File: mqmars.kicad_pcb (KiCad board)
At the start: 2 copper layers, 275 parts, among them Q1 GSFP6016, Q10 GSFP6016, Q11 GSFP6016, Q12 GSFP6016, Q13 GSFP6016, Q14 GSFP6016, Q15 GSFP6016, Q16 GSFP6016, Q17 GSFP6016, Q18 GSFP6016, Q19 GSFP6016, Q2 GSFP6016, Q20 GSFP6016, Q21 GSFP6016, Q22 GSFP6016, Q23 GSFP6016, Q24 GSFP6016, Q25 GSFP6016, Q26 GSFP6016, Q27 GSFP6016, Q28 GSFP6016, Q29 GSFP6016, Q3 GSFP6016, Q30 GSFP6016, Q31 GSFP6016, Q32 GSFP6016, Q33 GSFP6016, Q34 GSFP6016, Q35 GSFP6016, Q36 GSFP6016, Q37 BC846, Q38 BC846, Q39 G700P06D5, Q4 GSFP6016, Q40 G700P06D5, Q41 BC846, Q42 BC846, Q43 G700P06D5, Q44 G700P06D5, Q45 BC846, Q46 BC846, Q47 G700P06D5, Q48 G700P06D5, Q5 GSFP6016, Q6 GSFP6016, Q7 GSFP6016, Q8 GSFP6016, Q9 GSFP6016, U1 MCT8329A1IREER, U10 TCA9548APWR, U12 TPS56224, U13 LMV358, U2 MCT8329A1IREER, U3 MCT8329A1IREER, U4 MCT8329A1IREER, U5 MCT8329A1IREER, U6 MCT8329A1IREER, U8 MCP23017_SO, U9 TLA2528IRTER

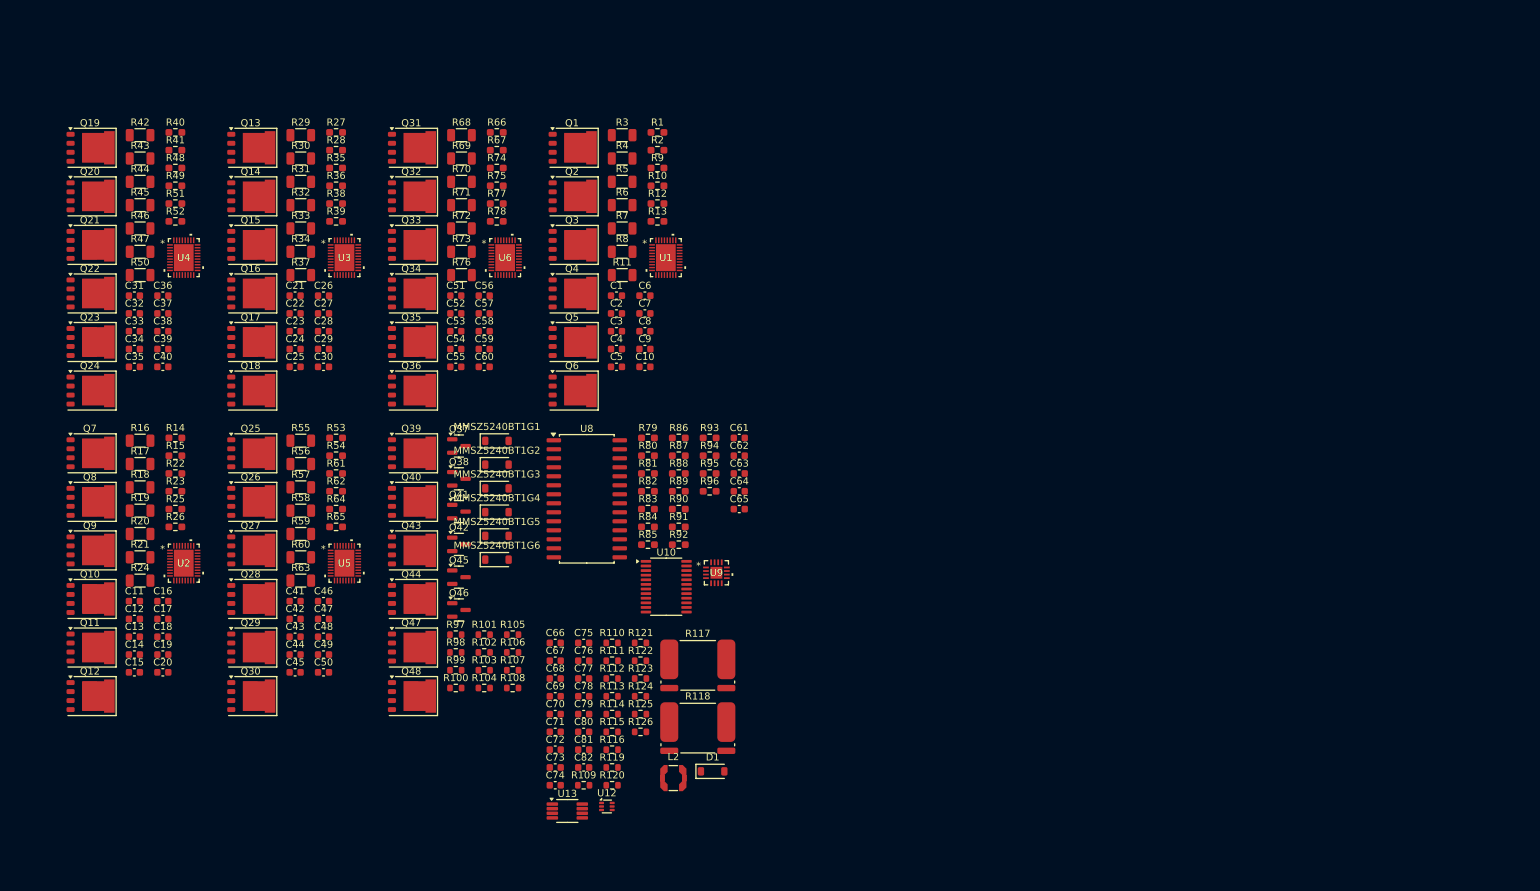
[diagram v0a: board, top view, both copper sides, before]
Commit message: Powerstage
Powerstage layout, non critical changes to schematic
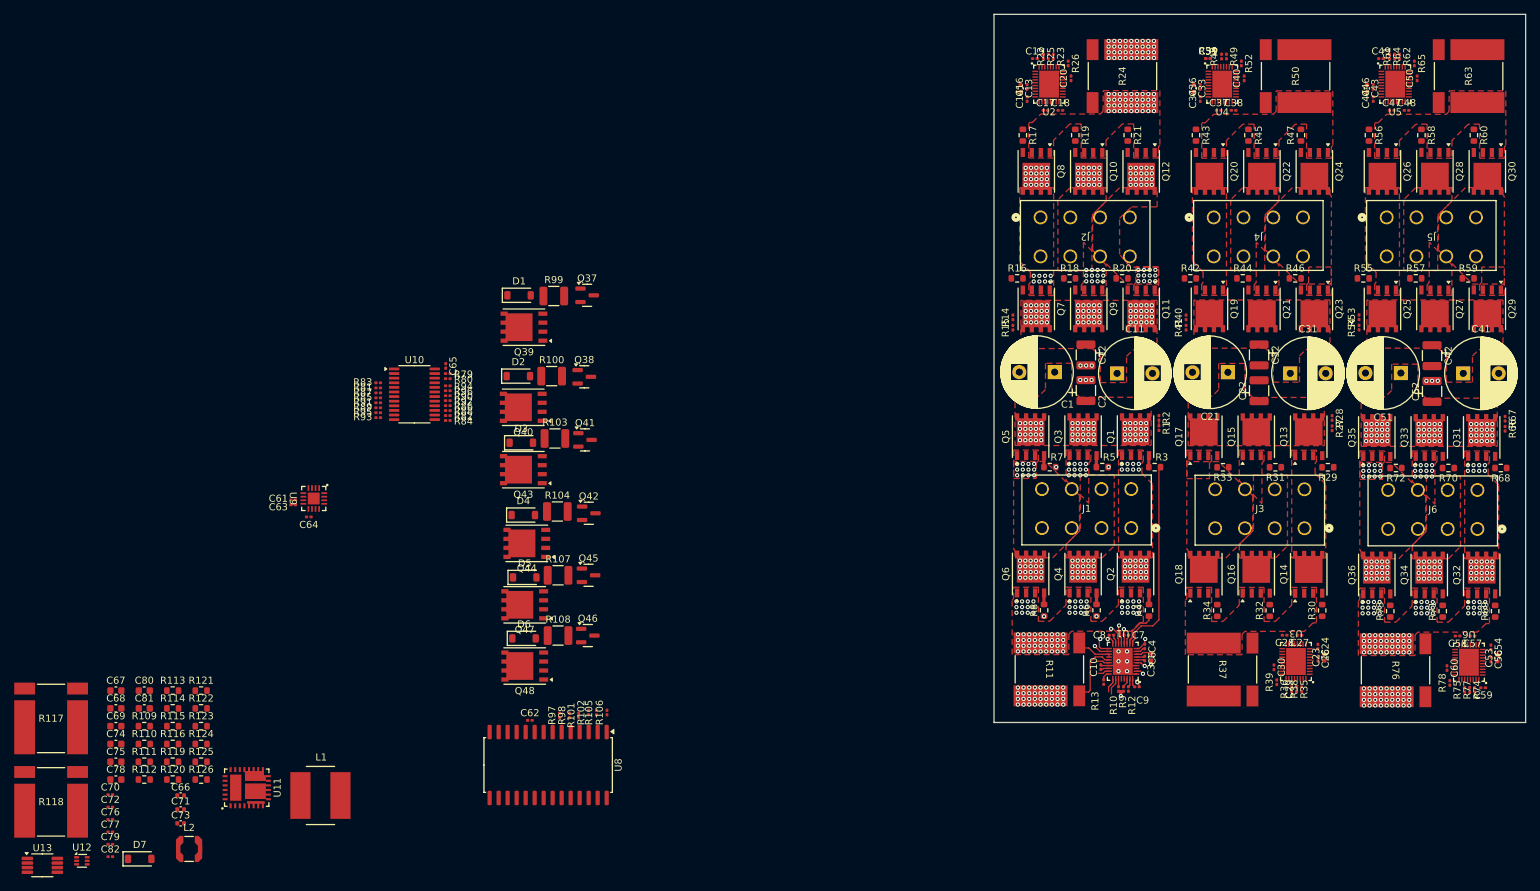
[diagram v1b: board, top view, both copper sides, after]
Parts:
- removed C15, C25, C35, C45, C5, C55: 100n, Capacitor_SMD:C_0603_1608Metric
- removed MMSZ5240BT1G1, MMSZ5240BT1G2, MMSZ5240BT1G3, MMSZ5240BT1G4, MMSZ5240BT1G5, MMSZ5240BT1G6: 10V1, Diode_SMD:D_SOD-123
- added D2: 10V1, Diode_SMD:D_SOD-123, F.Cu at (124.4, 76.5)
- added D3: 10V1, Diode_SMD:D_SOD-123, F.Cu at (124.8, 85.9)
- added D4: 10V1, Diode_SMD:D_SOD-123, F.Cu at (125.1, 96.1)
- added D5: 10V1, Diode_SMD:D_SOD-123, F.Cu at (125.3, 104.9)
- added D6: 10V1, Diode_SMD:D_SOD-123, F.Cu at (125.2, 113.5)
- added D7: SD103AW, Diode_SMD:D_SOD-123, F.Cu at (71.0, 144.6)
- added J1: 1724470408, footprints:CONN08_1724470408_MOL, F.Cu at (210.9, 98.0)
- added J2: 1724470408, footprints:CONN08_1724470408_MOL, F.Cu at (198.1, 54.1)
- added J3: 1724470408, footprints:CONN08_1724470408_MOL, F.Cu at (235.3, 98.0)
- added J4: 1724470408, footprints:CONN08_1724470408_MOL, F.Cu at (222.5, 54.1)
- added J5: 1724470408, footprints:CONN08_1724470408_MOL, F.Cu at (246.9, 54.1)
- added J6: 1724470408, footprints:CONN08_1724470408_MOL, F.Cu at (259.7, 98.1)
- added L1: 2.2u, Inductor_SMD:L_Bourns_SRN8040TA, F.Cu at (96.5, 135.7)
- added U11: MIC26903YJL-TR, footprints:MLF28_5X6_MCH, F.Cu at (86.1, 134.6)
- C1, C11, C21, C31, C41, C51: footprint Capacitor_SMD:C_0603_1608Metric -> Capacitor_THT:CP_Radial_D10.0mm_P5.00mm
- C10, C14, C16, C17, C18, C19, C20, C24, C26, C27, C28, C29, C30, C34, C36, C37, C38, C39, C4, C40, C44, C46, C47, C48, C49, C50, C54, C56, C57, C58, C59, C6, C60, C61, C62, C63, C64, C7, C70, C72, C76, C79, C8, C82, C9: footprint Capacitor_SMD:C_0603_1608Metric -> Capacitor_SMD:C_0201_0603Metric
- C12, C2, C22, C32, C42, C52: footprint Capacitor_SMD:C_0603_1608Metric -> Capacitor_SMD:C_1210_3225Metric
- C13, C23, C3, C33, C43, C53, C66, C71, C73: footprint Capacitor_SMD:C_0603_1608Metric -> Capacitor_SMD:C_0402_1005Metric
- C65: value 100n -> ~; footprint Capacitor_SMD:C_0603_1608Metric -> Capacitor_SMD:C_0201_0603Metric
- C77: value 4.7n -> ~; footprint Capacitor_SMD:C_0603_1608Metric -> Capacitor_SMD:C_0201_0603Metric
- D1: value SD103AW -> MMSZ5240BT1G5
- Q1, Q10, Q11, Q12, Q13, Q14, Q15, Q16, Q17, Q18, Q19, Q2, Q20, Q21, Q22, Q23, Q24, Q25, Q26, Q27, Q28, Q29, Q3, Q30, Q31, Q32, Q33, Q34, Q35, Q36, Q39, Q4, Q40, Q43, Q44, Q47, Q48, Q5, Q6, Q7, Q8, Q9: footprint Package_DFN_QFN:PQFN-8-EP_6x5mm_P1.27mm_Generic -> Package_SO:PowerPAK_SO-8_Single
- R1, R10, R12, R13, R14, R15, R2, R22, R23, R25, R26, R27, R28, R35, R36, R38, R39, R40, R41, R48, R49, R51, R52, R53, R54, R61, R62, R64, R65, R66, R67, R74, R75, R77, R78, R79, R80, R81, R82, R83, R84, R85, R86, R87, R88, R89, R9, R90, R91, R92, R93, R94, R95, R96: footprint Resistor_SMD:R_0603_1608Metric_Pad0.98x0.95mm_HandSolder -> Resistor_SMD:R_0201_0603Metric
- R100, R103, R104, R107, R108, R99: footprint Resistor_SMD:R_0603_1608Metric -> Resistor_SMD:R_1210_3225Metric
- R101, R102, R105, R106, R97, R98: footprint Resistor_SMD:R_0603_1608Metric -> Resistor_SMD:R_0201_0603Metric
- R11, R24, R37, R50, R63, R76: value 10m0R -> WSL3637R0100FEA; footprint Resistor_SMD:R_1206_3216Metric -> footprints:WSL3637_VIS
- R117, R118: value 10m0R -> WSL3637R0100FEA; footprint Resistor_SMD:R_Shunt_Isabellenhuette_BVR4026 -> footprints:WSL3637_VIS
- R16, R17, R18, R19, R20, R21, R29, R3, R30, R31, R32, R33, R34, R4, R42, R43, R44, R45, R46, R47, R5, R55, R56, R57, R58, R59, R6, R60, R68, R69, R7, R70, R71, R72, R73, R8: value 4.7R -> 4R7; footprint Resistor_SMD:R_1206_3216Metric -> Resistor_SMD:R_0603_1608Metric
- moved Q30 189.5 mm to (261.1, 47.7), turned to -90 degrees
- moved Q29 180.9 mm to (261.1, 67.0), turned to -90 degrees
- moved R63 179.5 mm to (258.5, 34.2), turned to 90 degrees
- moved Q28 177.6 mm to (253.7, 47.6), turned to -90 degrees
- moved R60 175.9 mm to (259.2, 42.5), turned to -90 degrees
- moved C50 175.6 mm to (251.2, 34.5), turned to 90 degrees
- moved Q24 175.5 mm to (236.7, 47.7), turned to -90 degrees
- moved Q23 172.8 mm to (236.7, 67.1), turned to -90 degrees
- moved C49 171.2 mm to (246.1, 31.7)
- moved C44 171.1 mm to (245.0, 37.4), turned to 90 degrees
- moved Q27 170.5 mm to (253.7, 67.1), turned to -90 degrees
- moved C48 169.9 mm to (249.7, 39.0)
- moved C43 169.8 mm to (244.1, 35.9), turned to -90 degrees
- moved R59 168.6 mm to (258.4, 62.7)
- moved C41 167.9 mm to (257.7, 76.1)
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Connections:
- C14 pad 1: Net-(J4-Pin_1) -> Net-(Q8-D)
- C16 pad 1: Net-(U2-CPL) -> Net-(U2-CPH)
- C16 pad 2: Net-(U2-CPH) -> Net-(U2-CPL)
- C17 pad 2: Net-(J5-Pin_1) -> Net-(Q10-D)
- C18 pad 2: Net-(J6-Pin_1) -> Net-(Q12-D)
- C24 pad 1: Net-(J7-Pin_1) -> Net-(Q14-D)
- C26 pad 1: Net-(U3-CPL) -> Net-(U3-CPH)
- C26 pad 2: Net-(U3-CPH) -> Net-(U3-CPL)
- C27 pad 2: Net-(J8-Pin_1) -> Net-(Q16-D)
- C28 pad 2: Net-(J9-Pin_1) -> Net-(Q18-D)
- C34 pad 1: Net-(J10-Pin_1) -> Net-(Q20-D)
- C36 pad 1: Net-(U4-CPL) -> Net-(U4-CPH)
- C36 pad 2: Net-(U4-CPH) -> Net-(U4-CPL)
- C37 pad 2: Net-(J11-Pin_1) -> Net-(Q22-D)
- C38 pad 2: Net-(J12-Pin_1) -> Net-(Q24-D)
- C4 pad 1: Net-(J1-Pin_1) -> Net-(Q2-D)
- C41 pad 1: Net-(U5-PVDD) -> RC_{VDD}
- C42 pad 1: Net-(U5-PVDD) -> RC_{VDD}
- C44 pad 1: Net-(J13-Pin_1) -> Net-(Q26-D)
- C46 pad 1: Net-(U5-CPL) -> Net-(U5-CPH)
- C46 pad 2: Net-(U5-CPH) -> Net-(U5-CPL)
- C47 pad 2: Net-(J14-Pin_1) -> Net-(Q28-D)
- C48 pad 2: Net-(J15-Pin_1) -> Net-(Q30-D)
- C54 pad 1: Net-(J16-Pin_1) -> Net-(Q32-D)
- C56 pad 1: Net-(U6-CPL) -> Net-(U6-CPH)
- C56 pad 2: Net-(U6-CPH) -> Net-(U6-CPL)
- C57 pad 2: Net-(J17-Pin_1) -> Net-(Q34-D)
- C58 pad 2: Net-(J18-Pin_1) -> Net-(Q36-D)
- C6 pad 1: Net-(U1-CPL) -> Net-(U1-CPH)
- C6 pad 2: Net-(U1-CPH) -> Net-(U1-CPL)
- C7 pad 2: Net-(J2-Pin_1) -> Net-(Q4-D)
- C70 pad 1: Net-(D1-K) -> Net-(D7-K)
- C73 pad 2: Net-(D1-A) -> Net-(D7-A)
- C8 pad 2: Net-(J3-Pin_1) -> Net-(Q6-D)
- D1 pad 1: Net-(D1-K) -> +BATT
- Q1 pad 1: +BATT -> Net-(Q2-D)
- Q1 pad 2: Net-(Q1-G) -> Net-(Q2-D)
- Q1 pad 3: Net-(J1-Pin_1) -> Net-(Q2-D)
- Q1 pad 4: (no net) -> Net-(Q1-G)
- Q1 pad 5: (no net) -> LF_{VDD}
- Q10 pad 1: Net-(J5-Pin_1) -> Net-(Q10-S-Pad1)
- Q10 pad 2: Net-(Q10-G) -> Net-(Q10-S-Pad1)
- Q10 pad 3: Net-(Q10-S) -> Net-(Q10-S-Pad1)
- Q10 pad 4: (no net) -> Net-(Q10-G)
- Q10 pad 5: (no net) -> Net-(Q10-D)
- Q11 pad 1: +BATT -> Net-(Q12-D)
- Q11 pad 2: Net-(Q11-G) -> Net-(Q12-D)
- Q11 pad 3: Net-(J6-Pin_1) -> Net-(Q12-D)
- Q11 pad 4: (no net) -> Net-(Q11-G)
- Q11 pad 5: (no net) -> LC_{VDD}
- Q12 pad 1: Net-(J6-Pin_1) -> Net-(Q10-S-Pad1)
- Q12 pad 2: Net-(Q12-G) -> Net-(Q10-S-Pad1)
- Q12 pad 3: Net-(Q10-S) -> Net-(Q10-S-Pad1)
- Q12 pad 4: (no net) -> Net-(Q12-G)
- Q12 pad 5: (no net) -> Net-(Q12-D)
- Q13 pad 1: +BATT -> Net-(Q14-D)
- Q13 pad 2: Net-(Q13-G) -> Net-(Q14-D)
- Q13 pad 3: Net-(J7-Pin_1) -> Net-(Q14-D)
- Q13 pad 4: (no net) -> Net-(Q13-G)
- Q13 pad 5: (no net) -> LR_{VDD}
- Q14 pad 1: Net-(J7-Pin_1) -> Net-(Q14-S-Pad1)
- Q14 pad 2: Net-(Q14-G) -> Net-(Q14-S-Pad1)
- Q14 pad 3: Net-(Q14-S) -> Net-(Q14-S-Pad1)
- Q14 pad 4: (no net) -> Net-(Q14-G)
- Q14 pad 5: (no net) -> Net-(Q14-D)
- Q15 pad 1: +BATT -> Net-(Q16-D)
- Q15 pad 2: Net-(Q15-G) -> Net-(Q16-D)
- Q15 pad 3: Net-(J8-Pin_1) -> Net-(Q16-D)
- Q15 pad 4: (no net) -> Net-(Q15-G)
- Q15 pad 5: (no net) -> LR_{VDD}
- Q16 pad 1: Net-(J8-Pin_1) -> Net-(Q14-S-Pad1)
- Q16 pad 2: Net-(Q16-G) -> Net-(Q14-S-Pad1)
- Q16 pad 3: Net-(Q14-S) -> Net-(Q14-S-Pad1)
- Q16 pad 4: (no net) -> Net-(Q16-G)
- Q16 pad 5: (no net) -> Net-(Q16-D)
- Q17 pad 1: +BATT -> Net-(Q18-D)
- Q17 pad 2: Net-(Q17-G) -> Net-(Q18-D)
- Q17 pad 3: Net-(J9-Pin_1) -> Net-(Q18-D)
- Q17 pad 4: (no net) -> Net-(Q17-G)
- Q17 pad 5: (no net) -> LR_{VDD}
- Q18 pad 1: Net-(J9-Pin_1) -> Net-(Q14-S-Pad1)
- Q18 pad 2: Net-(Q18-G) -> Net-(Q14-S-Pad1)
- Q18 pad 3: Net-(Q14-S) -> Net-(Q14-S-Pad1)
- Q18 pad 4: (no net) -> Net-(Q18-G)
- Q18 pad 5: (no net) -> Net-(Q18-D)
- Q19 pad 1: +BATT -> Net-(Q20-D)
- Q19 pad 2: Net-(Q19-G) -> Net-(Q20-D)
- Q19 pad 3: Net-(J10-Pin_1) -> Net-(Q20-D)
- Q19 pad 4: (no net) -> Net-(Q19-G)
- Q19 pad 5: (no net) -> RF_{VDD}
- Q2 pad 1: Net-(J1-Pin_1) -> Net-(Q2-S-Pad1)
- Q2 pad 2: Net-(Q2-G) -> Net-(Q2-S-Pad1)
- Q2 pad 3: Net-(Q2-S) -> Net-(Q2-S-Pad1)
- Q2 pad 4: (no net) -> Net-(Q2-G)
- Q2 pad 5: (no net) -> Net-(Q2-D)
- Q20 pad 1: Net-(J10-Pin_1) -> Net-(Q20-S-Pad1)
- Q20 pad 2: Net-(Q20-G) -> Net-(Q20-S-Pad1)
- Q20 pad 3: Net-(Q20-S) -> Net-(Q20-S-Pad1)
- Q20 pad 4: (no net) -> Net-(Q20-G)
- Q20 pad 5: (no net) -> Net-(Q20-D)
- Q21 pad 1: +BATT -> Net-(Q22-D)
- Q21 pad 2: Net-(Q21-G) -> Net-(Q22-D)
- Q21 pad 3: Net-(J11-Pin_1) -> Net-(Q22-D)
- Q21 pad 4: (no net) -> Net-(Q21-G)
- Q21 pad 5: (no net) -> RF_{VDD}
- Q22 pad 1: Net-(J11-Pin_1) -> Net-(Q20-S-Pad1)
- Q22 pad 2: Net-(Q22-G) -> Net-(Q20-S-Pad1)
- Q22 pad 3: Net-(Q20-S) -> Net-(Q20-S-Pad1)
- Q22 pad 4: (no net) -> Net-(Q22-G)
- Q22 pad 5: (no net) -> Net-(Q22-D)
- Q23 pad 1: +BATT -> Net-(Q24-D)
- Q23 pad 2: Net-(Q23-G) -> Net-(Q24-D)
- Q23 pad 3: Net-(J12-Pin_1) -> Net-(Q24-D)
- Q23 pad 4: (no net) -> Net-(Q23-G)
- Q23 pad 5: (no net) -> RF_{VDD}
- Q24 pad 1: Net-(J12-Pin_1) -> Net-(Q20-S-Pad1)
- Q24 pad 2: Net-(Q24-G) -> Net-(Q20-S-Pad1)
- Q24 pad 3: Net-(Q20-S) -> Net-(Q20-S-Pad1)
- Q24 pad 4: (no net) -> Net-(Q24-G)
- Q24 pad 5: (no net) -> Net-(Q24-D)
- Q25 pad 1: +BATT -> Net-(Q26-D)
- Q25 pad 2: Net-(Q25-G) -> Net-(Q26-D)
- Q25 pad 3: Net-(J13-Pin_1) -> Net-(Q26-D)
- Q25 pad 4: (no net) -> Net-(Q25-G)
- Q25 pad 5: (no net) -> RC_{VDD}
- Q26 pad 1: Net-(J13-Pin_1) -> Net-(Q26-S-Pad1)
- Q26 pad 2: Net-(Q26-G) -> Net-(Q26-S-Pad1)
- Q26 pad 3: Net-(Q26-S) -> Net-(Q26-S-Pad1)
- Q26 pad 4: (no net) -> Net-(Q26-G)
- Q26 pad 5: (no net) -> Net-(Q26-D)
- Q27 pad 1: +BATT -> Net-(Q28-D)
- Q27 pad 2: Net-(Q27-G) -> Net-(Q28-D)
- Q27 pad 3: Net-(J14-Pin_1) -> Net-(Q28-D)
- Q27 pad 4: (no net) -> Net-(Q27-G)
- Q27 pad 5: (no net) -> RC_{VDD}
- Q28 pad 1: Net-(J14-Pin_1) -> Net-(Q26-S-Pad1)
- Q28 pad 2: Net-(Q28-G) -> Net-(Q26-S-Pad1)
- Q28 pad 3: Net-(Q26-S) -> Net-(Q26-S-Pad1)
- Q28 pad 4: (no net) -> Net-(Q28-G)
- Q28 pad 5: (no net) -> Net-(Q28-D)
- Q29 pad 1: +BATT -> Net-(Q30-D)
- Q29 pad 2: Net-(Q29-G) -> Net-(Q30-D)
- Q29 pad 3: Net-(J15-Pin_1) -> Net-(Q30-D)
- Q29 pad 4: (no net) -> Net-(Q29-G)
- Q29 pad 5: (no net) -> RC_{VDD}
- Q3 pad 1: +BATT -> Net-(Q4-D)
- Q3 pad 2: Net-(Q3-G) -> Net-(Q4-D)
- Q3 pad 3: Net-(J2-Pin_1) -> Net-(Q4-D)
- Q3 pad 4: (no net) -> Net-(Q3-G)
- Q3 pad 5: (no net) -> LF_{VDD}
- Q30 pad 1: Net-(J15-Pin_1) -> Net-(Q26-S-Pad1)
- Q30 pad 2: Net-(Q30-G) -> Net-(Q26-S-Pad1)
- Q30 pad 3: Net-(Q26-S) -> Net-(Q26-S-Pad1)
- Q30 pad 4: (no net) -> Net-(Q30-G)
- Q30 pad 5: (no net) -> Net-(Q30-D)
- Q31 pad 1: +BATT -> Net-(Q32-D)
- Q31 pad 2: Net-(Q31-G) -> Net-(Q32-D)
- Q31 pad 3: Net-(J16-Pin_1) -> Net-(Q32-D)
- Q31 pad 4: (no net) -> Net-(Q31-G)
- Q31 pad 5: (no net) -> RR_{VDD}
- Q32 pad 1: Net-(J16-Pin_1) -> Net-(Q32-S-Pad1)
- Q32 pad 2: Net-(Q32-G) -> Net-(Q32-S-Pad1)
- Q32 pad 3: Net-(Q32-S) -> Net-(Q32-S-Pad1)
- Q32 pad 4: (no net) -> Net-(Q32-G)
- Q32 pad 5: (no net) -> Net-(Q32-D)
- Q33 pad 1: +BATT -> Net-(Q34-D)
- Q33 pad 2: Net-(Q33-G) -> Net-(Q34-D)
- Q33 pad 3: Net-(J17-Pin_1) -> Net-(Q34-D)
- Q33 pad 4: (no net) -> Net-(Q33-G)
- Q33 pad 5: (no net) -> RR_{VDD}
- Q34 pad 1: Net-(J17-Pin_1) -> Net-(Q32-S-Pad1)
- Q34 pad 2: Net-(Q34-G) -> Net-(Q32-S-Pad1)
- Q34 pad 3: Net-(Q32-S) -> Net-(Q32-S-Pad1)
- Q34 pad 4: (no net) -> Net-(Q34-G)
- Q34 pad 5: (no net) -> Net-(Q34-D)
- Q35 pad 1: +BATT -> Net-(Q36-D)
- Q35 pad 2: Net-(Q35-G) -> Net-(Q36-D)
- Q35 pad 3: Net-(J18-Pin_1) -> Net-(Q36-D)
- Q35 pad 4: (no net) -> Net-(Q35-G)
- Q35 pad 5: (no net) -> RR_{VDD}
- Q36 pad 1: Net-(J18-Pin_1) -> Net-(Q32-S-Pad1)
- Q36 pad 2: Net-(Q36-G) -> Net-(Q32-S-Pad1)
- Q36 pad 3: Net-(Q32-S) -> Net-(Q32-S-Pad1)
- Q36 pad 4: (no net) -> Net-(Q36-G)
- Q36 pad 5: (no net) -> Net-(Q36-D)
- Q39 pad 2: Net-(MMSZ5240BT1G1-A) -> LF_{VDD}
- Q39 pad 3: +BATT -> LF_{VDD}
- Q39 pad 4: (no net) -> Net-(D1-A)
- Q39 pad 5: (no net) -> +BATT
- Q4 pad 1: Net-(J2-Pin_1) -> Net-(Q2-S-Pad1)
- Q4 pad 2: Net-(Q4-G) -> Net-(Q2-S-Pad1)
- Q4 pad 3: Net-(Q2-S) -> Net-(Q2-S-Pad1)
- Q4 pad 4: (no net) -> Net-(Q4-G)
- Q4 pad 5: (no net) -> Net-(Q4-D)
- Q40 pad 2: Net-(MMSZ5240BT1G2-A) -> RF_{VDD}
- Q40 pad 3: +BATT -> RF_{VDD}
- Q40 pad 4: (no net) -> Net-(D2-A)
- Q40 pad 5: (no net) -> +BATT
- Q43 pad 2: Net-(MMSZ5240BT1G3-A) -> LC_{VDD}
- Q43 pad 3: +BATT -> LC_{VDD}
- Q43 pad 4: (no net) -> Net-(D3-A)
- Q43 pad 5: (no net) -> +BATT
- Q44 pad 2: Net-(MMSZ5240BT1G4-A) -> RC_{VDD}
- Q44 pad 3: +BATT -> RC_{VDD}
- Q44 pad 4: (no net) -> Net-(D4-A)
- Q44 pad 5: (no net) -> +BATT
- Q47 pad 2: Net-(MMSZ5240BT1G5-A) -> LR_{VDD}
- Q47 pad 3: +BATT -> LR_{VDD}
- Q47 pad 4: (no net) -> Net-(D5-A)
- Q47 pad 5: (no net) -> +BATT
- Q48 pad 2: Net-(MMSZ5240BT1G6-A) -> RR_{VDD}
- Q48 pad 3: +BATT -> RR_{VDD}
- Q48 pad 4: (no net) -> Net-(D6-A)
- Q48 pad 5: (no net) -> +BATT
- Q5 pad 1: +BATT -> Net-(Q6-D)
- Q5 pad 2: Net-(Q5-G) -> Net-(Q6-D)
- Q5 pad 3: Net-(J3-Pin_1) -> Net-(Q6-D)
- Q5 pad 4: (no net) -> Net-(Q5-G)
- Q5 pad 5: (no net) -> LF_{VDD}
- Q6 pad 1: Net-(J3-Pin_1) -> Net-(Q2-S-Pad1)
- Q6 pad 2: Net-(Q6-G) -> Net-(Q2-S-Pad1)
- Q6 pad 3: Net-(Q2-S) -> Net-(Q2-S-Pad1)
- Q6 pad 4: (no net) -> Net-(Q6-G)
- Q6 pad 5: (no net) -> Net-(Q6-D)
- Q7 pad 1: +BATT -> Net-(Q8-D)
- Q7 pad 2: Net-(Q7-G) -> Net-(Q8-D)
- Q7 pad 3: Net-(J4-Pin_1) -> Net-(Q8-D)
- Q7 pad 4: (no net) -> Net-(Q7-G)
- Q7 pad 5: (no net) -> LC_{VDD}
- Q8 pad 1: Net-(J4-Pin_1) -> Net-(Q10-S-Pad1)
- Q8 pad 2: Net-(Q8-G) -> Net-(Q10-S-Pad1)
- Q8 pad 3: Net-(Q10-S) -> Net-(Q10-S-Pad1)
- Q8 pad 4: (no net) -> Net-(Q8-G)
- Q8 pad 5: (no net) -> Net-(Q8-D)
- Q9 pad 1: +BATT -> Net-(Q10-D)
- Q9 pad 2: Net-(Q9-G) -> Net-(Q10-D)
- Q9 pad 3: Net-(J5-Pin_1) -> Net-(Q10-D)
- Q9 pad 4: (no net) -> Net-(Q9-G)
- Q9 pad 5: (no net) -> LC_{VDD}
- R100 pad 1: Net-(MMSZ5240BT1G2-A) -> Net-(D2-A)
- R103 pad 1: Net-(MMSZ5240BT1G3-A) -> Net-(D3-A)
- R104 pad 1: Net-(MMSZ5240BT1G4-A) -> Net-(D4-A)
- R107 pad 1: Net-(MMSZ5240BT1G5-A) -> Net-(D5-A)
- R108 pad 1: Net-(MMSZ5240BT1G6-A) -> Net-(D6-A)
- R11 pad 1: Net-(Q2-S) -> Net-(Q2-S-Pad1)
- R11 pad 2: GNDPWR -> Net-(U1-LSS)
- R110 pad 2: Net-(D1-A) -> Net-(D7-A)
- R117 pad 2: +3.3V -> Net-(R117-Pad2)
- R117 pad 3: (no net) -> Net-(R117-Pad3)
- R117 pad 4: (no net) -> +3.3V
- R118 pad 1: Net-(C75-Pad2) -> +5V
- R118 pad 2: +5V -> Net-(R118-Pad2)
- R118 pad 3: (no net) -> Net-(R118-Pad3)
- R118 pad 4: (no net) -> Net-(C75-Pad2)
- R119 pad 1: +3.3V -> Net-(R117-Pad3)
- R120 pad 1: Net-(C79-Pad1) -> Net-(R117-Pad2)
- R121 pad 1: Net-(C75-Pad2) -> Net-(R118-Pad3)
- R122 pad 1: +5V -> Net-(R118-Pad2)
- R24 pad 1: Net-(Q10-S) -> Net-(Q10-S-Pad1)
- R24 pad 2: GNDPWR -> Net-(U2-LSS)
- R37 pad 1: Net-(Q14-S) -> Net-(Q14-S-Pad1)
- R37 pad 2: GNDPWR -> Net-(U3-LSS)
- R50 pad 1: Net-(Q20-S) -> Net-(Q20-S-Pad1)
- R50 pad 2: GNDPWR -> Net-(U4-LSS)
- R54 pad 1: Net-(U5-PVDD) -> RC_{VDD}
- R63 pad 1: Net-(Q26-S) -> Net-(Q26-S-Pad1)
- R63 pad 2: GNDPWR -> Net-(U5-LSS)
- R76 pad 1: Net-(Q32-S) -> Net-(Q32-S-Pad1)
- R76 pad 2: GNDPWR -> Net-(U6-LSS)
- R99 pad 1: Net-(MMSZ5240BT1G1-A) -> Net-(D1-A)
- U1 pad 10: Net-(J1-Pin_1) -> Net-(Q2-D)
- U1 pad 14: Net-(J2-Pin_1) -> Net-(Q4-D)
- U1 pad 18: Net-(J3-Pin_1) -> Net-(Q6-D)
- U1 pad 21: Net-(Q2-S) -> Net-(U1-LSS)
- U1 pad 22: Net-(Q2-S) -> Net-(U1-LSS)
- U1 pad 23: GNDPWR -> Net-(U1-SN)
- U2 pad 10: Net-(J4-Pin_1) -> Net-(Q8-D)
- U2 pad 14: Net-(J5-Pin_1) -> Net-(Q10-D)
- U2 pad 18: Net-(J6-Pin_1) -> Net-(Q12-D)
- U2 pad 21: Net-(Q10-S) -> Net-(U2-LSS)
- U2 pad 22: Net-(Q10-S) -> Net-(U2-LSS)
- U2 pad 23: GNDPWR -> Net-(U2-SN)
- U3 pad 10: Net-(J7-Pin_1) -> Net-(Q14-D)
- U3 pad 14: Net-(J8-Pin_1) -> Net-(Q16-D)
- U3 pad 18: Net-(J9-Pin_1) -> Net-(Q18-D)
- U3 pad 21: Net-(Q14-S) -> Net-(U3-LSS)
- U3 pad 22: Net-(Q14-S) -> Net-(U3-LSS)
- U3 pad 23: GNDPWR -> Net-(U3-SN)
- U4 pad 10: Net-(J10-Pin_1) -> Net-(Q20-D)
- U4 pad 14: Net-(J11-Pin_1) -> Net-(Q22-D)
- U4 pad 18: Net-(J12-Pin_1) -> Net-(Q24-D)
- U4 pad 21: Net-(Q20-S) -> Net-(U4-LSS)
- U4 pad 22: Net-(Q20-S) -> Net-(U4-LSS)
- U4 pad 23: GNDPWR -> Net-(U4-SN)
- U5 pad 10: Net-(J13-Pin_1) -> Net-(Q26-D)
- U5 pad 14: Net-(J14-Pin_1) -> Net-(Q28-D)
- U5 pad 18: Net-(J15-Pin_1) -> Net-(Q30-D)
- U5 pad 21: Net-(Q26-S) -> Net-(U5-LSS)
- U5 pad 22: Net-(Q26-S) -> Net-(U5-LSS)
- U5 pad 23: GNDPWR -> Net-(U5-SN)
- U5 pad 5: Net-(U5-PVDD) -> RC_{VDD}
- U6 pad 10: Net-(J16-Pin_1) -> Net-(Q32-D)
- U6 pad 14: Net-(J17-Pin_1) -> Net-(Q34-D)
- U6 pad 18: Net-(J18-Pin_1) -> Net-(Q36-D)
- U6 pad 21: Net-(Q32-S) -> Net-(U6-LSS)
- U6 pad 22: Net-(Q32-S) -> Net-(U6-LSS)
- U6 pad 23: GNDPWR -> Net-(U6-SN)
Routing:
- net Net-(U1-GHC): track 0.00 -> 31.9 mm, vias 0 -> 2
- net Net-(U1-GHA): track 0.00 -> 27.6 mm
- net Net-(U1-GHB): track 0.00 -> 26.3 mm, vias 0 -> 2
- net Net-(Q6-D): track 0.00 -> 19.6 mm, vias 0 -> 33
- net Net-(Q2-D): track 0.00 -> 13.1 mm, vias 0 -> 29
- net Net-(Q4-D): track 0.00 -> 12.5 mm, vias 0 -> 33
- net Net-(U1-GLC): track 0.00 -> 12.4 mm, vias 0 -> 2
- net GND: track 0.00 -> 12.0 mm, vias 0 -> 18
- net Net-(U1-SN): track 0.00 -> 8.31 mm
- net Net-(U1-GLB): track 0.00 -> 5.99 mm, vias 0 -> 2
- net Net-(U1-LSS): track 0.00 -> 5.76 mm
- net Net-(U1-GLA): track 0.00 -> 5.53 mm
- net LF_{VDD}: track 0.00 -> 2.91 mm, vias 0 -> 61
- net SCL_{LF}: track 0.00 -> 2.40 mm
- net SDA_{LF}: track 0.00 -> 2.10 mm
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- added copper zone on F.Cu, net LC_{VDD}
- added copper zone on In1.Cu, net LC_{VDD}
- added copper zone on F.Cu, net LF_{VDD}
- added copper zone on In1.Cu, net LF_{VDD}
- added copper zone on F.Cu, net LR_{VDD}
- added copper zone on In1.Cu, net LR_{VDD}
- added copper zone on F.Cu, net Net-(Q10-D)
- added copper zone on In1.Cu, net Net-(Q10-D)
- added copper zone on F.Cu, net Net-(Q10-S-Pad1)
- added copper zone on In1.Cu, net Net-(Q10-S-Pad1)
- added copper zone on F.Cu, net Net-(Q12-D)
- added copper zone on In1.Cu, net Net-(Q12-D)
- added copper zone on F.Cu, net Net-(Q14-D)
- added copper zone on In1.Cu, net Net-(Q14-D)
- added copper zone on F.Cu, net Net-(Q14-S-Pad1)
- added copper zone on In1.Cu, net Net-(Q14-S-Pad1)
- added copper zone on F.Cu, net Net-(Q16-D)
- added copper zone on In1.Cu, net Net-(Q16-D)
- added copper zone on F.Cu, net Net-(Q18-D)
- added copper zone on In1.Cu, net Net-(Q18-D)
- added copper zone on F.Cu, net Net-(Q2-D)
- added copper zone on In1.Cu, net Net-(Q2-D)
- added copper zone on F.Cu, net Net-(Q2-S-Pad1)
- added copper zone on In1.Cu, net Net-(Q2-S-Pad1)
- added copper zone on F.Cu, net Net-(Q20-D)
- added copper zone on In1.Cu, net Net-(Q20-D)
- added copper zone on F.Cu, net Net-(Q20-S-Pad1)
- added copper zone on In1.Cu, net Net-(Q20-S-Pad1)
- added copper zone on F.Cu, net Net-(Q22-D)
- added copper zone on In1.Cu, net Net-(Q22-D)
- added copper zone on F.Cu, net Net-(Q24-D)
- added copper zone on In1.Cu, net Net-(Q24-D)
- added copper zone on F.Cu, net Net-(Q26-D)
- added copper zone on In1.Cu, net Net-(Q26-D)
- added copper zone on F.Cu, net Net-(Q26-S-Pad1)
- added copper zone on In1.Cu, net Net-(Q26-S-Pad1)
- added copper zone on F.Cu, net Net-(Q28-D)
- added copper zone on In1.Cu, net Net-(Q28-D)
- added copper zone on F.Cu, net Net-(Q30-D)
- added copper zone on In1.Cu, net Net-(Q30-D)
- added copper zone on F.Cu, net Net-(Q32-D)
- added copper zone on In1.Cu, net Net-(Q32-D)
- added copper zone on F.Cu, net Net-(Q32-S-Pad1)
- added copper zone on In1.Cu, net Net-(Q32-S-Pad1)
- added copper zone on F.Cu, net Net-(Q34-D)
- added copper zone on In1.Cu, net Net-(Q34-D)
- added copper zone on F.Cu, net Net-(Q36-D)
- added copper zone on In1.Cu, net Net-(Q36-D)
- added copper zone on F.Cu, net Net-(Q4-D)
- added copper zone on In1.Cu, net Net-(Q4-D)
- added copper zone on F.Cu, net Net-(Q6-D)
- added copper zone on In1.Cu, net Net-(Q6-D)
- added copper zone on F.Cu, net Net-(Q8-D)
- added copper zone on In1.Cu, net Net-(Q8-D)
- added copper zone on F.Cu, net RC_{VDD}
- added copper zone on In1.Cu, net RC_{VDD}
- added copper zone on F.Cu, net RF_{VDD}
- added copper zone on In1.Cu, net RF_{VDD}
- added copper zone on F.Cu, net RR_{VDD}
- added copper zone on In1.Cu, net RR_{VDD}
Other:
- board outline added: 75 x 99.9 mm
- copper layers 2 -> 4
